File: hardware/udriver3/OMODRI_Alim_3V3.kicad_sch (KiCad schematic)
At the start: 10 parts, among them U13 MPM3804GG

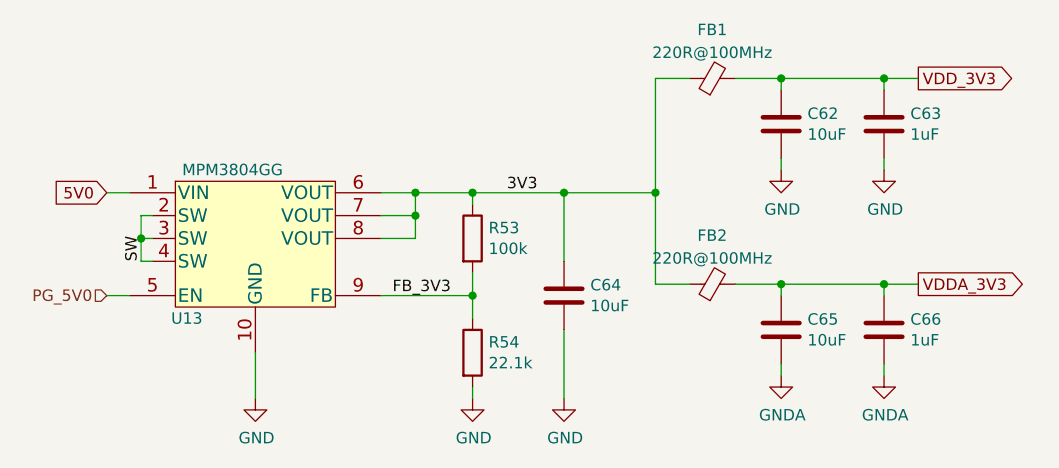
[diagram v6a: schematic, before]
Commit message: PCB udpates. - add serial resistors on boot jumpers - modify config jumpers to be opened by default
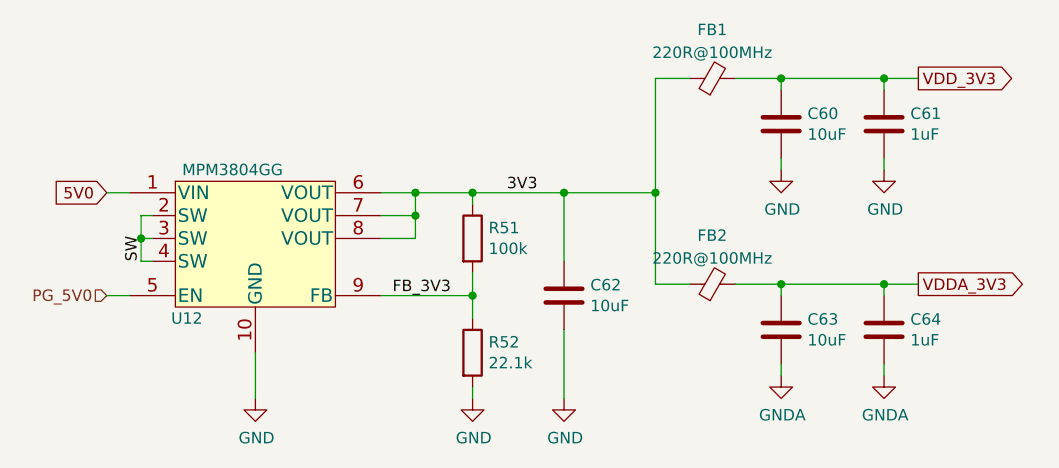
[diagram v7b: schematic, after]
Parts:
- renumbered C62 to C60, C63 to C61, C64 to C62, C65 to C63, C66 to C64, R53 to R51, R54 to R52, U13 to U12
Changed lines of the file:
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@@
   (symbol (lib_id "power:GND") (at 113.03 110.49 0) (unit 1)
     (in_bom yes) (on_board yes)
-    (property "Reference" "#PWR0136" (id 0) (at 113.03 116.84 0)
+    (property "Reference" "#PWR0122" (id 0) (at 113.03 116.84 0)
       (effects (font (size 1.27 1.27)) hide)
     )
@@
   (symbol (lib_id "power:GND") (at 147.32 110.49 0) (unit 1)
     (in_bom yes) (on_board yes)
-    (property "Reference" "#PWR0138" (id 0) (at 147.32 116.84 0)
+    (property "Reference" "#PWR0124" (id 0) (at 147.32 116.84 0)
       (effects (font (size 1.27 1.27)) hide)
     )
@@
   (symbol (lib_id "power:GND") (at 137.16 110.49 0) (unit 1)
     (in_bom yes) (on_board yes)
-    (property "Reference" "#PWR0137" (id 0) (at 137.16 116.84 0)
+    (property "Reference" "#PWR0123" (id 0) (at 137.16 116.84 0)
       (effects (font (size 1.27 1.27)) hide)
     )
@@
   (symbol (lib_id "Device:R") (at 137.16 92.71 0) (unit 1)
     (in_bom yes) (on_board yes)
-    (property "Reference" "R53" (id 0) (at 138.938 91.5416 0)
+    (property "Reference" "R51" (id 0) (at 138.938 91.5416 0)
       (effects (font (size 1.27 1.27)) (justify left))
     )
@@
   (symbol (lib_id "Device:R") (at 137.16 105.41 0) (unit 1)
     (in_bom yes) (on_board yes)
-    (property "Reference" "R54" (id 0) (at 138.938 104.2416 0)
+    (property "Reference" "R52" (id 0) (at 138.938 104.2416 0)
       (effects (font (size 1.27 1.27)) (justify left))
     )
@@
   (symbol (lib_id "omodri_lib:MPM3804GG") (at 113.03 93.98 0) (unit 1)
     (in_bom yes) (on_board yes)
-    (property "Reference" "U13" (id 0) (at 105.41 101.6 0))
+    (property "Reference" "U12" (id 0) (at 105.41 101.6 0))
     (property "Value" "MPM3804GG" (id 1) (at 110.49 85.09 0))
     (property "Footprint" "udriver3:QFN-10_2x2mm_P0.5mm" (id 2) (at 113.03 93.98 0)
@@
   (symbol (lib_id "Device:C") (at 147.32 99.06 0) (unit 1)
     (in_bom yes) (on_board yes)
-    (property "Reference" "C64" (id 0) (at 150.241 97.8916 0)
+    (property "Reference" "C62" (id 0) (at 150.241 97.8916 0)
       (effects (font (size 1.27 1.27)) (justify left))
     )
@@
   (symbol (lib_id "Device:C") (at 171.45 80.01 0) (unit 1)
     (in_bom yes) (on_board yes)
-    (property "Reference" "C62" (id 0) (at 174.371 78.8416 0)
+    (property "Reference" "C60" (id 0) (at 174.371 78.8416 0)
       (effects (font (size 1.27 1.27)) (justify left))
     )
@@
   (symbol (lib_id "Device:C") (at 182.88 80.01 0) (unit 1)
     (in_bom yes) (on_board yes)
-    (property "Reference" "C63" (id 0) (at 185.801 78.8416 0)
+    (property "Reference" "C61" (id 0) (at 185.801 78.8416 0)
       (effects (font (size 1.27 1.27)) (justify left))
     )
@@
   (symbol (lib_id "power:GND") (at 171.45 85.09 0) (unit 1)
     (in_bom yes) (on_board yes)
-    (property "Reference" "#PWR0132" (id 0) (at 171.45 91.44 0)
+    (property "Reference" "#PWR0118" (id 0) (at 171.45 91.44 0)
       (effects (font (size 1.27 1.27)) hide)
     )
@@
   (symbol (lib_id "power:GND") (at 182.88 85.09 0) (unit 1)
     (in_bom yes) (on_board yes)
-    (property "Reference" "#PWR0133" (id 0) (at 182.88 91.44 0)
+    (property "Reference" "#PWR0119" (id 0) (at 182.88 91.44 0)
       (effects (font (size 1.27 1.27)) hide)
     )
@@
   (symbol (lib_id "Device:C") (at 171.45 102.87 0) (unit 1)
     (in_bom yes) (on_board yes)
-    (property "Reference" "C65" (id 0) (at 174.371 101.7016 0)
+    (property "Reference" "C63" (id 0) (at 174.371 101.7016 0)
       (effects (font (size 1.27 1.27)) (justify left))
     )
@@
   (symbol (lib_id "Device:C") (at 182.88 102.87 0) (unit 1)
     (in_bom yes) (on_board yes)
-    (property "Reference" "C66" (id 0) (at 185.801 101.7016 0)
+    (property "Reference" "C64" (id 0) (at 185.801 101.7016 0)
       (effects (font (size 1.27 1.27)) (justify left))
     )
@@
   (symbol (lib_id "power:GNDA") (at 171.45 107.95 0) (unit 1)
     (in_bom yes) (on_board yes)
-    (property "Reference" "#PWR0134" (id 0) (at 171.45 114.3 0)
+    (property "Reference" "#PWR0120" (id 0) (at 171.45 114.3 0)
       (effects (font (size 1.27 1.27)) hide)
     )
@@
   (symbol (lib_id "power:GNDA") (at 182.88 107.95 0) (unit 1)
     (in_bom yes) (on_board yes)
-    (property "Reference" "#PWR0135" (id 0) (at 182.88 114.3 0)
-      (effects (font (size 1.27 1.27)) hide)
-    )
+    (property "Reference" "#PWR0121" (id 0) (at 182.88 114.3 0)
+      (effects (font (size 1.27 1.27)) hide)
+    )
